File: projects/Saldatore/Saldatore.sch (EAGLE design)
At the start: 28 parts, among them IC1 7805TV, IC2 LM358N, Q1 IRF540, Q2 2N2905, T1 TIP73

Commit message: in lavoro saldatore.
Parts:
- removed C1, C2: (no value), rcl:C-EU025-025X050
- removed HEATER: SMKDSP_1,5/3, con-phoenix-smkdsp:SMKDSP_1,5/3
- removed IC1: 7805TV, linear:7805TV
- removed TEMP: S2B-XH-A(LF)(SN), Connectors:S2B-XH-A(LF)(SN)
- added D2: 5v1-2W, diode_MOD:ZENER-DIODEDO41Z10
- added R4: 47-2W, rcl:R-EU_0204/7
- added SOLDERING: (no value), con-lstb:MA05-1
- R1: value (none) -> 270
- R12, R3: device rcl:R-TRIMM3339P -> rcl:R-TRIMM64W
- R2: value (none) -> 10k
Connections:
- net N$21 renamed ENC_CLK
- net N$22 renamed ENC_DT
- net N$23 renamed ENC_SW
- net N$24 renamed 3V3
- removed net 5V: 10K.2, C2.1, IC1.VO, U$1.5V
- new net 5V1: 10K.2, D2.C, R4.1, U$1.5V
- net 24V: now also R4.2, SOLDERING.1; no longer C1.1, HEATER-3.KL, IC1.VI
- net GND: now also D2.A, SOLDERING.3, SOLDERING.5; no longer C1.2, C2.2, HEATER-1.KL, IC1.GND, TEMP.1
- net HEATER-: now also SOLDERING.2; no longer HEATER-2.KL
- net TEMP+: now also SOLDERING.4; no longer TEMP.2

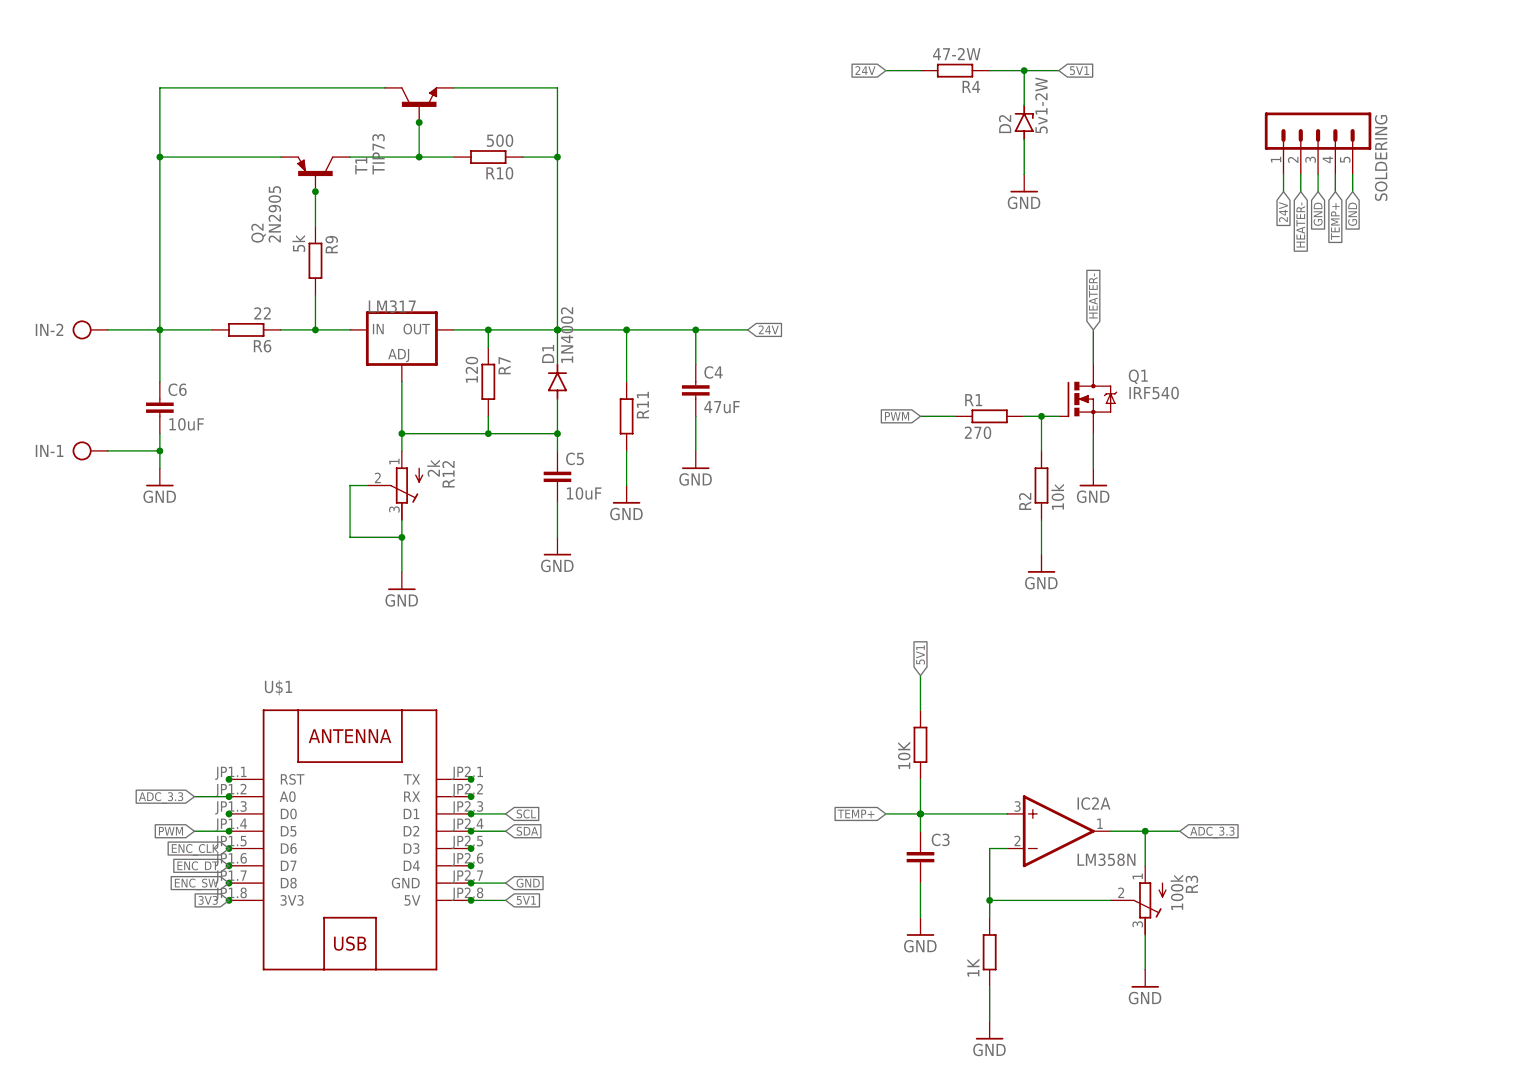
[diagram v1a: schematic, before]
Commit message: terminato schema saldatore. esportate immagini.
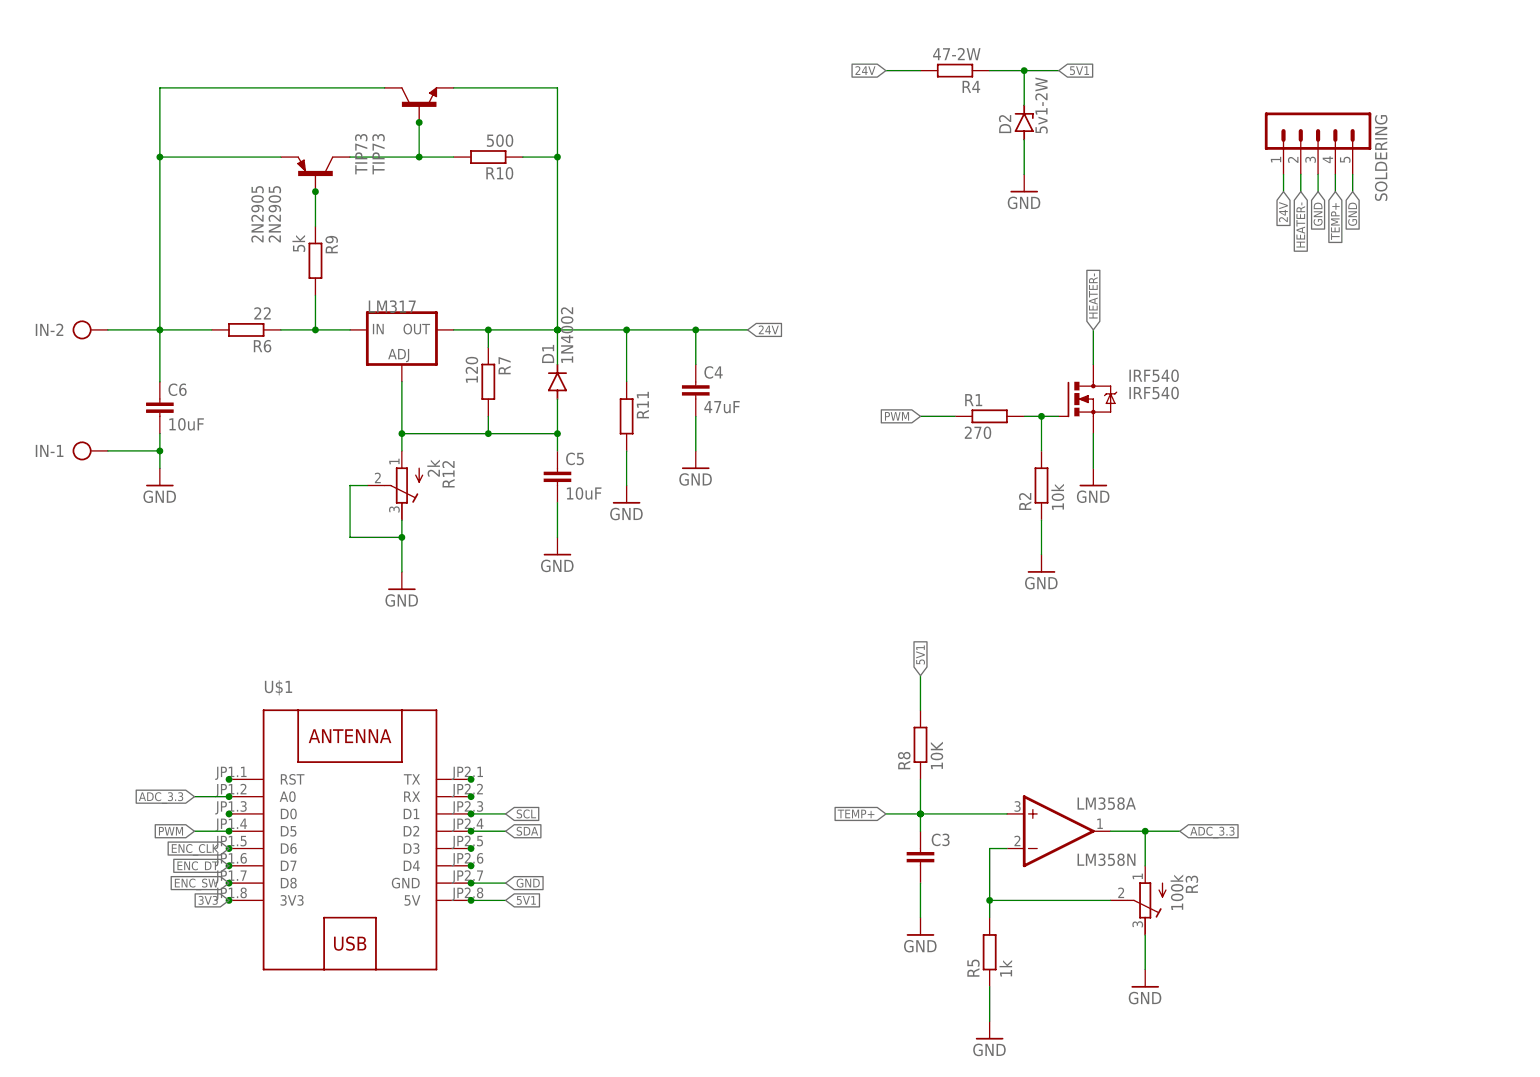
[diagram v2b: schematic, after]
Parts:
- R5: value (none) -> 1k
- R8: value (none) -> 10K
- renumbered 10K to R8, 1K to R5, IC2 to LM358, Q1 to IRF540, Q2 to 2N2905, T1 to TIP73
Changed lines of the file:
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@@
 <?xml version="1.0" encoding="utf-8"?>
 <!DOCTYPE eagle SYSTEM "eagle.dtd">
-<eagle version="9.5.0">
+<eagle version="9.5.1">
 <drawing>
 <settings>
@@
 </classes>
 <parts>
-<part name="Q1" library="transistor-power" library_urn="urn:adsk.eagle:library:400" deviceset="IRF540" device="" package3d_urn="urn:adsk.eagle:package:29484/3"/>
+<part name="IRF540" library="transistor-power" library_urn="urn:adsk.eagle:library:400" deviceset="IRF540" device="" package3d_urn="urn:adsk.eagle:package:29484/3"/>
 <part name="R1" library="rcl" library_urn="urn:adsk.eagle:library:334" deviceset="R-EU_" device="0204/7" package3d_urn="urn:adsk.eagle:package:23498/2" value="270"/>
 <part name="R2" library="rcl" library_urn="urn:adsk.eagle:library:334" deviceset="R-EU_" device="0204/7" package3d_urn="urn:adsk.eagle:package:23498/2" value="10k"/>
-<part name="10K" library="rcl" library_urn="urn:adsk.eagle:library:334" deviceset="R-EU_" device="0204/7" package3d_urn="urn:adsk.eagle:package:23498/2"/>
-<part name="1K" library="rcl" library_urn="urn:adsk.eagle:library:334" deviceset="R-EU_" device="0204/7" package3d_urn="urn:adsk.eagle:package:23498/2"/>
-<part name="IC2" library="linear" library_urn="urn:adsk.eagle:library:262" deviceset="LM358" device="N" package3d_urn="urn:adsk.eagle:package:16409/2"/>
+<part name="R8" library="rcl" library_urn="urn:adsk.eagle:library:334" deviceset="R-EU_" device="0204/7" package3d_urn="urn:adsk.eagle:package:23498/2" value="10K"/>
+<part name="R5" library="rcl" library_urn="urn:adsk.eagle:library:334" deviceset="R-EU_" device="0204/7" package3d_urn="urn:adsk.eagle:package:23498/2" value="1k"/>
+<part name="LM358" library="linear" library_urn="urn:adsk.eagle:library:262" deviceset="LM358" device="N" package3d_urn="urn:adsk.eagle:package:16409/2"/>
 <part name="GND1" library="supply1" library_urn="urn:adsk.eagle:library:371" deviceset="GND" device=""/>
 <part name="GND2" library="supply1" library_urn="urn:adsk.eagle:library:371" deviceset="GND" device=""/>
@@
 <part name="C6" library="rcl" library_urn="urn:adsk.eagle:library:334" deviceset="C-EU" device="025-025X050" package3d_urn="urn:adsk.eagle:package:23629/2" value="10uF"/>
 <part name="R9" library="rcl" library_urn="urn:adsk.eagle:library:334" deviceset="R-EU_" device="0204/7" package3d_urn="urn:adsk.eagle:package:23498/2" value="5k"/>
-<part name="Q2" library="transistor-pnp" library_urn="urn:adsk.eagle:library:399" deviceset="2N2905*" device="" package3d_urn="urn:adsk.eagle:package:28730/1"/>
-<part name="T1" library="transistor" library_urn="urn:adsk.eagle:library:402" deviceset="2N1613" device="" package3d_urn="urn:adsk.eagle:package:28729/1" value="TIP73"/>
+<part name="2N2905" library="transistor-pnp" library_urn="urn:adsk.eagle:library:399" deviceset="2N2905*" device="" package3d_urn="urn:adsk.eagle:package:28730/1"/>
+<part name="TIP73" library="transistor" library_urn="urn:adsk.eagle:library:402" deviceset="2N1613" device="" package3d_urn="urn:adsk.eagle:package:28729/1" value="TIP73"/>
 <part name="R10" library="rcl" library_urn="urn:adsk.eagle:library:334" deviceset="R-EU_" device="0204/7" package3d_urn="urn:adsk.eagle:package:23498/2" value="500"/>
 <part name="R11" library="rcl" library_urn="urn:adsk.eagle:library:334" deviceset="R-EU_" device="0204/7" package3d_urn="urn:adsk.eagle:package:23498/2"/>
@@
 </plain>
 <instances>
-<instance part="Q1" gate="G$1" x="55.88" y="35.56" smashed="yes">
+<instance part="IRF540" gate="G$1" x="55.88" y="35.56" smashed="yes">
 <attribute name="NAME" x="63.5" y="38.1" size="1.778" layer="95"/>
 <attribute name="VALUE" x="63.5" y="35.56" size="1.778" layer="96"/>
@@
 <attribute name="VALUE" x="54.102" y="19.05" size="1.778" layer="96" rot="R90"/>
 </instance>
-<instance part="10K" gate="G$1" x="33.02" y="-15.24" smashed="yes" rot="R90">
+<instance part="R8" gate="G$1" x="33.02" y="-15.24" smashed="yes" rot="R90">
 <attribute name="NAME" x="31.5214" y="-19.05" size="1.778" layer="95" rot="R90"/>
 <attribute name="VALUE" x="36.322" y="-19.05" size="1.778" layer="96" rot="R90"/>
 </instance>
-<instance part="1K" gate="G$1" x="43.18" y="-45.72" smashed="yes" rot="R90">
+<instance part="R5" gate="G$1" x="43.18" y="-45.72" smashed="yes" rot="R90">
 <attribute name="NAME" x="41.6814" y="-49.53" size="1.778" layer="95" rot="R90"/>
 <attribute name="VALUE" x="46.482" y="-49.53" size="1.778" layer="96" rot="R90"/>
 </instance>
-<instance part="IC2" gate="A" x="53.34" y="-27.94" smashed="yes">
+<instance part="LM358" gate="A" x="53.34" y="-27.94" smashed="yes">
 <attribute name="NAME" x="55.88" y="-24.765" size="1.778" layer="95"/>
 <attribute name="VALUE" x="55.88" y="-33.02" size="1.778" layer="96"/>
@@
 <attribute name="VALUE" x="-59.182" y="59.69" size="1.778" layer="96" rot="R270"/>
 </instance>
-<instance part="Q2" gate="G$1" x="-55.88" y="68.58" smashed="yes" rot="R90">
+<instance part="2N2905" gate="G$1" x="-55.88" y="68.58" smashed="yes" rot="R90">
 <attribute name="NAME" x="-63.5" y="58.42" size="1.778" layer="95" rot="R90"/>
 <attribute name="VALUE" x="-60.96" y="58.42" size="1.778" layer="96" rot="R90"/>
 </instance>
-<instance part="T1" gate="G$1" x="-40.64" y="78.74" smashed="yes" rot="R90">
+<instance part="TIP73" gate="G$1" x="-40.64" y="78.74" smashed="yes" rot="R90">
 <attribute name="NAME" x="-48.26" y="68.58" size="1.778" layer="95" rot="R90"/>
 <attribute name="VALUE" x="-45.72" y="68.58" size="1.778" layer="96" rot="R90"/>
@@
 <wire x1="-10.16" y1="38.1" x2="-10.16" y2="45.72" width="0.1524" layer="91"/>
 <junction x="-10.16" y="45.72"/>
-<pinref part="T1" gate="G$1" pin="E"/>
+<pinref part="TIP73" gate="G$1" pin="E"/>
 <wire x1="-35.56" y1="81.28" x2="-20.32" y2="81.28" width="0.1524" layer="91"/>
 <wire x1="-20.32" y1="81.28" x2="-20.32" y2="71.12" width="0.1524" layer="91"/>
@@
 </segment>
 <segment>
-<pinref part="10K" gate="G$1" pin="2"/>
+<pinref part="R8" gate="G$1" pin="2"/>
 <wire x1="33.02" y1="-10.16" x2="33.02" y2="-5.08" width="0.1524" layer="91"/>
 <label x="33.02" y="-5.08" size="1.27" layer="95" rot="R90" xref="yes"/>
@@
 </segment>
 <segment>
-<pinref part="Q1" gate="G$1" pin="S"/>
+<pinref part="IRF540" gate="G$1" pin="S"/>
 <wire x1="58.42" y1="30.48" x2="58.42" y2="25.4" width="0.1524" layer="91"/>
 <pinref part="GND2" gate="1" pin="GND"/>
@@
 </segment>
 <segment>
-<pinref part="1K" gate="G$1" pin="1"/>
+<pinref part="R5" gate="G$1" pin="1"/>
 <pinref part="GND10" gate="1" pin="GND"/>
 <wire x1="43.18" y1="-55.88" x2="43.18" y2="-50.8" width="0.1524" layer="91"/>
@@
 <segment>
 <pinref part="R1" gate="G$1" pin="2"/>
-<pinref part="Q1" gate="G$1" pin="G"/>
+<pinref part="IRF540" gate="G$1" pin="G"/>
 <wire x1="48.26" y1="33.02" x2="50.8" y2="33.02" width="0.1524" layer="91"/>
 <pinref part="R2" gate="G$1" pin="2"/>
@@
 <pinref part="R3" gate="G$1" pin="S"/>
 <wire x1="60.96" y1="-38.1" x2="43.18" y2="-38.1" width="0.1524" layer="91"/>
-<pinref part="1K" gate="G$1" pin="2"/>
+<pinref part="R5" gate="G$1" pin="2"/>
 <wire x1="43.18" y1="-38.1" x2="43.18" y2="-40.64" width="0.1524" layer="91"/>
-<pinref part="IC2" gate="A" pin="-IN"/>
+<pinref part="LM358" gate="A" pin="-IN"/>
 <wire x1="45.72" y1="-30.48" x2="43.18" y2="-30.48" width="0.1524" layer="91"/>
 <wire x1="43.18" y1="-30.48" x2="43.18" y2="-38.1" width="0.1524" layer="91"/>
@@
 <net name="ADC_3.3" class="0">
 <segment>
-<pinref part="IC2" gate="A" pin="OUT"/>
+<pinref part="LM358" gate="A" pin="OUT"/>
 <wire x1="60.96" y1="-27.94" x2="66.04" y2="-27.94" width="0.1524" layer="91"/>
 <label x="71.12" y="-27.94" size="1.27" layer="95" xref="yes"/>
@@
 <wire x1="33.02" y1="-25.4" x2="27.94" y2="-25.4" width="0.1524" layer="91"/>
 <label x="27.94" y="-25.4" size="1.27" layer="95" rot="R180" xref="yes"/>
-<pinref part="10K" gate="G$1" pin="1"/>
+<pinref part="R8" gate="G$1" pin="1"/>
 <wire x1="33.02" y1="-20.32" x2="33.02" y2="-25.4" width="0.1524" layer="91"/>
-<pinref part="IC2" gate="A" pin="+IN"/>
+<pinref part="LM358" gate="A" pin="+IN"/>
 <wire x1="33.02" y1="-25.4" x2="45.72" y2="-25.4" width="0.1524" layer="91"/>
 <junction x="33.02" y="-25.4"/>
@@
 <net name="HEATER-" class="0">
 <segment>
-<pinref part="Q1" gate="G$1" pin="D"/>
+<pinref part="IRF540" gate="G$1" pin="D"/>
 <wire x1="58.42" y1="40.64" x2="58.42" y2="45.72" width="0.1524" layer="91"/>
 <label x="58.42" y="45.72" size="1.27" layer="95" rot="R90" xref="yes"/>
@@
 <segment>
 <pinref part="R9" gate="G$1" pin="1"/>
-<pinref part="Q2" gate="G$1" pin="B"/>
+<pinref part="2N2905" gate="G$1" pin="B"/>
 <junction x="-55.88" y="66.04"/>
 <wire x1="-55.88" y1="66.04" x2="-55.88" y2="60.96" width="0.1524" layer="91"/>
@@
 <net name="N$7" class="0">
 <segment>
-<pinref part="T1" gate="G$1" pin="B"/>
-<pinref part="Q2" gate="G$1" pin="C"/>
+<pinref part="TIP73" gate="G$1" pin="B"/>
+<pinref part="2N2905" gate="G$1" pin="C"/>
 <pinref part="R10" gate="G$1" pin="2"/>
 <wire x1="-50.8" y1="71.12" x2="-40.64" y2="71.12" width="0.1524" layer="91"/>
@@
 <pinref part="R6" gate="G$1" pin="2"/>
 <pinref part="C6" gate="G$1" pin="1"/>
-<pinref part="Q2" gate="G$1" pin="E"/>
+<pinref part="2N2905" gate="G$1" pin="E"/>
 <wire x1="-60.96" y1="71.12" x2="-78.74" y2="71.12" width="0.1524" layer="91"/>
 <wire x1="-78.74" y1="71.12" x2="-78.74" y2="45.72" width="0.1524" layer="91"/>
-<pinref part="T1" gate="G$1" pin="C"/>
+<pinref part="TIP73" gate="G$1" pin="C"/>
 <wire x1="-45.72" y1="81.28" x2="-78.74" y2="81.28" width="0.1524" layer="91"/>
 <wire x1="-78.74" y1="81.28" x2="-78.74" y2="71.12" width="0.1524" layer="91"/>
